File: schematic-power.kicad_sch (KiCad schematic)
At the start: 25 parts, among them IC2 LM76202QPWPRQ1, U9 TPS62933

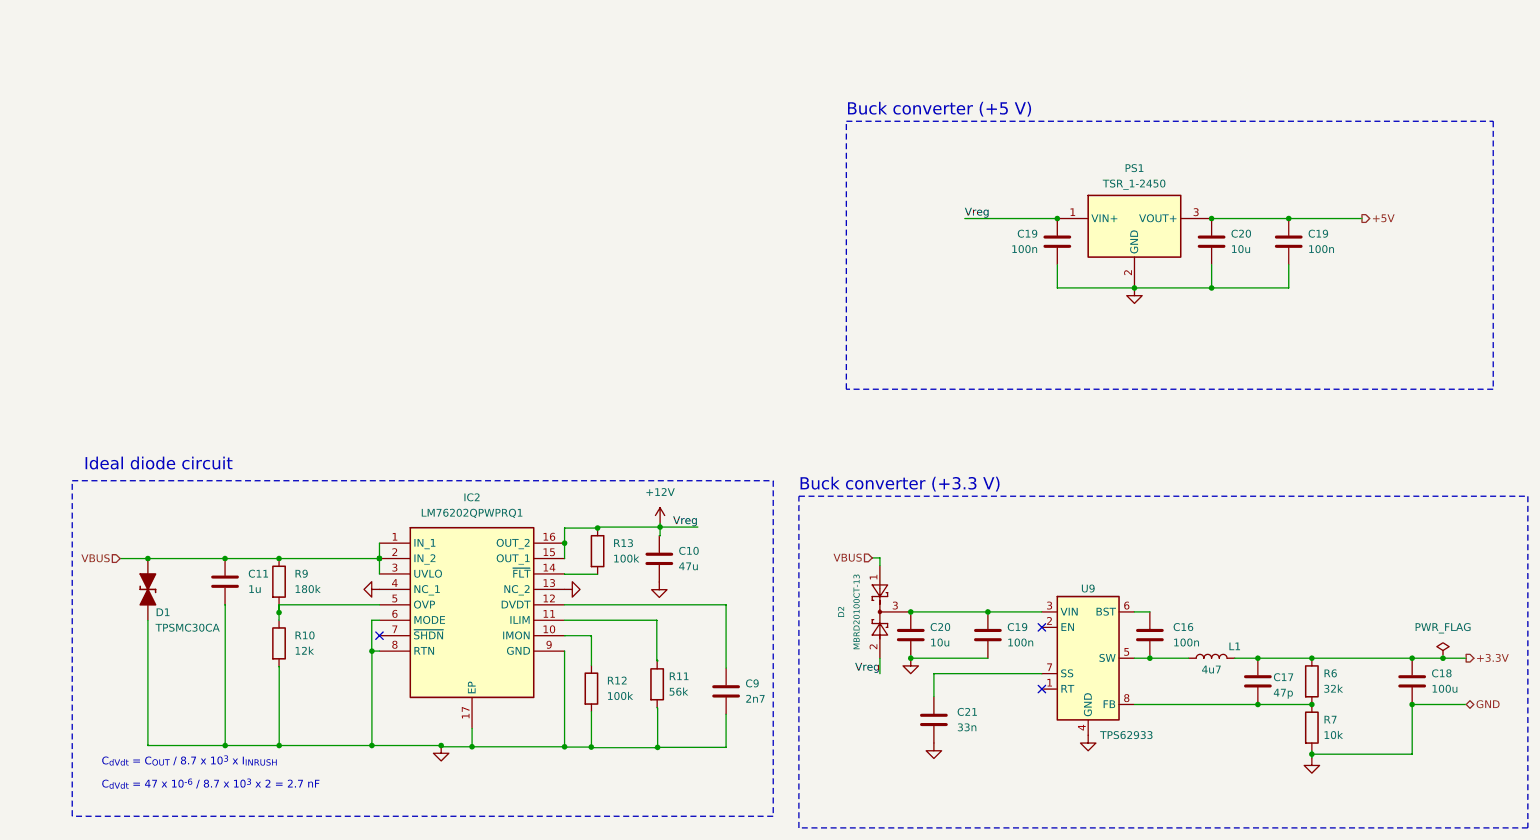
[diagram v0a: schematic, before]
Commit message: Add footprints, Placing MCU
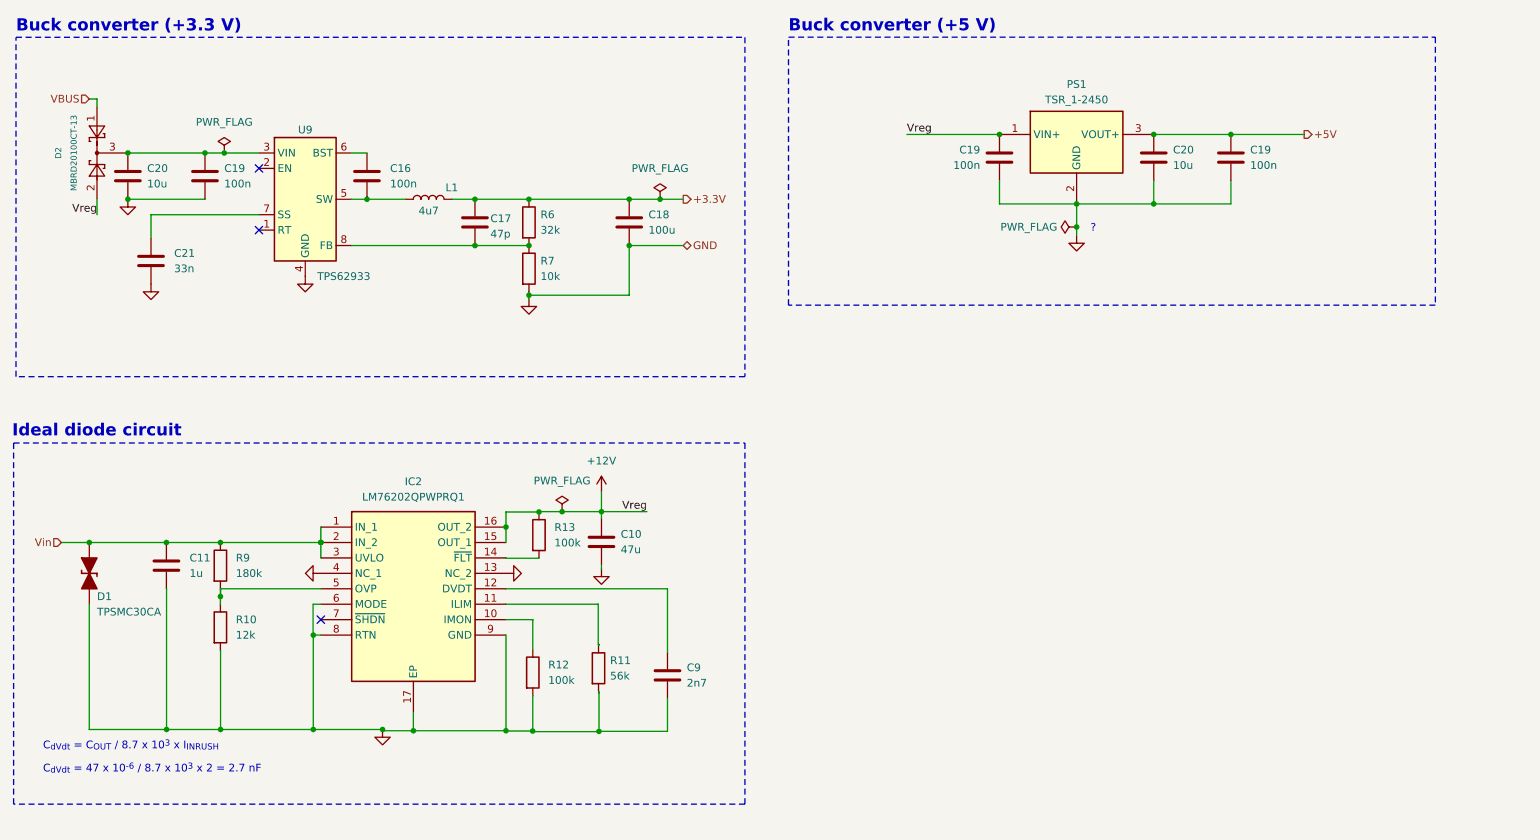
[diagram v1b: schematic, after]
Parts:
- PS1: footprint TSR-1-24120 -> Converter_DCDC:TSR-1-24120
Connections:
- net VBUS: no longer C11.1, D1.2 (A), IC2.1 (IN_1), IC2.2 (IN_2), IC2.3 (UVLO), R9.1
- new net Vin: C11.1, D1.2 (A), IC2.1 (IN_1), IC2.2 (IN_2), IC2.3 (UVLO), R9.1
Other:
- note added: "?"
- moved on the sheet: C10, C11, C16, C17, C18, C19, C20, C21, C9, D1, D2, IC2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
